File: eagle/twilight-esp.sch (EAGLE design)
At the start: 12 parts, among them J1 Mini PIR, J2 VOUT, J3 VIN, Q1 IRF540, U1 7805

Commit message: add led
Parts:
- added D1: (no value), SparkFun-LED:LED3MM
- added R5: 220R, resistor:R-EU_0204/5
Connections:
- new net N$6: R5.1, WEMOS1.D2
- new net N$7: D1.C, R5.2
- net 3.3V: now also D1.A
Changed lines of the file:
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@@
 <part name="SUPPLY8" library="SparkFun-PowerSymbols" deviceset="12V" device=""/>
 <part name="GND8" library="SparkFun-PowerSymbols" deviceset="GND" device=""/>
+<part name="R5" library="resistor" deviceset="R-EU_" device="0204/5" value="220R"/>
+<part name="D1" library="SparkFun-LED" deviceset="LED" device="3MM"/>
+<part name="SUPPLY9" library="SparkFun-PowerSymbols" deviceset="3.3V" device=""/>
 </parts>
 <sheets>
@@
 <instance part="SUPPLY8" gate="G$1" x="-2.54" y="45.72"/>
 <instance part="GND8" gate="1" x="-2.54" y="33.02"/>
+<instance part="R5" gate="G$1" x="68.58" y="76.2" rot="R90"/>
+<instance part="D1" gate="G$1" x="68.58" y="86.36"/>
+<instance part="SUPPLY9" gate="G$1" x="68.58" y="88.9"/>
 </instances>
 <busses>
@@
 <wire x1="15.24" y1="68.58" x2="15.24" y2="71.12" width="0.1524" layer="91"/>
 </segment>
+<segment>
+<wire x1="17.78" y1="60.96" x2="17.78" y2="63.5" width="0.1524" layer="91"/>
+</segment>
 </net>
 <net name="N$3" class="0">
@@
 <pinref part="SUPPLY2" gate="G$1" pin="3.3V"/>
 </segment>
+<segment>
+<pinref part="D1" gate="G$1" pin="A"/>
+<pinref part="SUPPLY9" gate="G$1" pin="3.3V"/>
+</segment>
 </net>
 <net name="5V" class="0">
@@
 </segment>
 </net>
+<net name="N$6" class="0">
+<segment>
+<pinref part="WEMOS1" gate="D1" pin="D2"/>
+<pinref part="R5" gate="G$1" pin="1"/>
+<wire x1="60.96" y1="71.12" x2="68.58" y2="71.12" width="0.1524" layer="91"/>
+</segment>
+</net>
+<net name="N$7" class="0">
+<segment>
+<pinref part="R5" gate="G$1" pin="2"/>
+<pinref part="D1" gate="G$1" pin="C"/>
+</segment>
+</net>

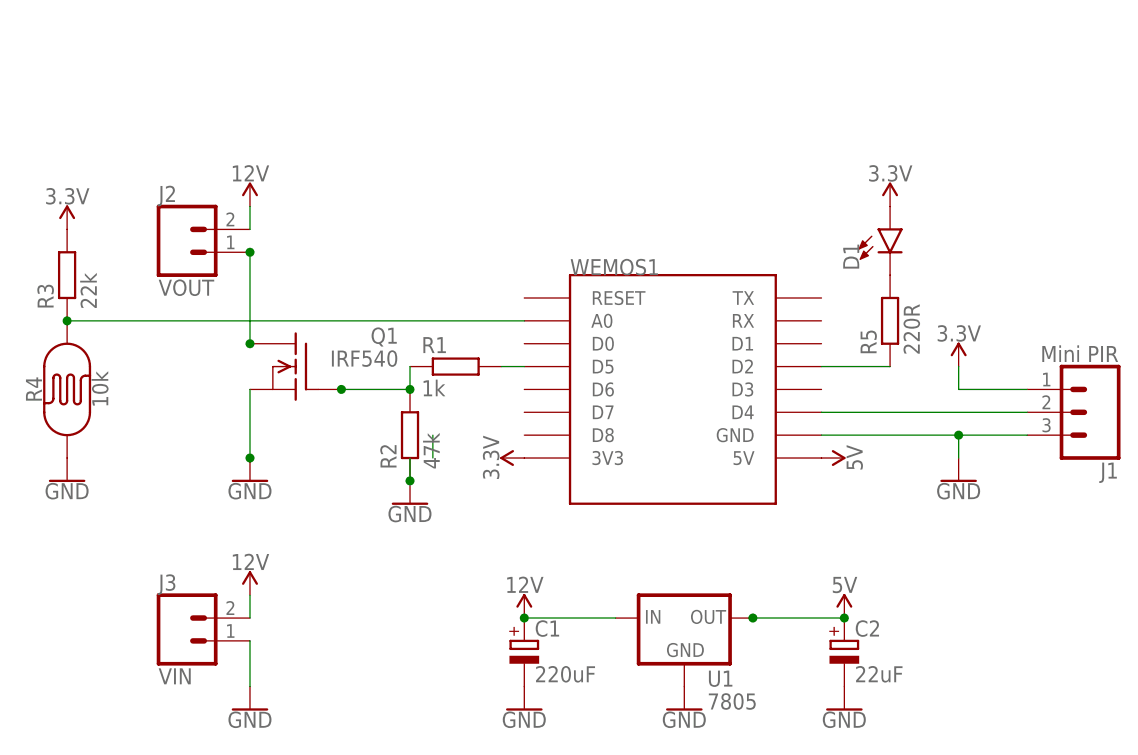
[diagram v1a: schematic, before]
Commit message: update schematic
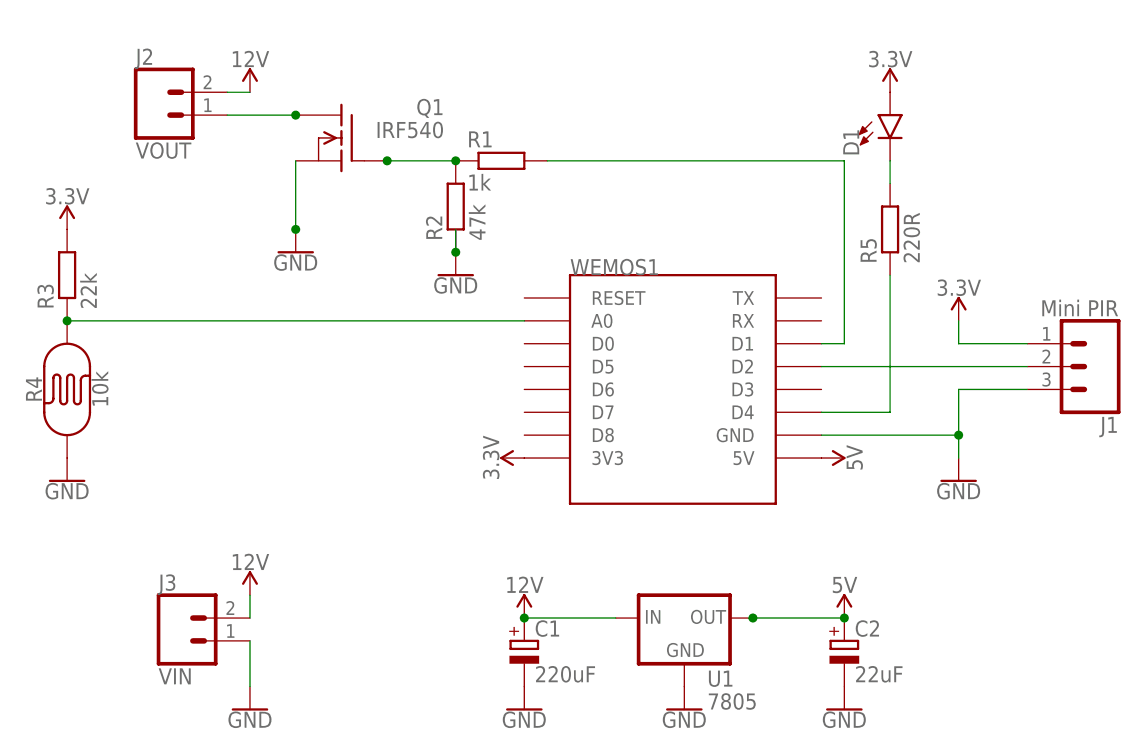
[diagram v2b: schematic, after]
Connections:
- net N$1: now also WEMOS1.D1; no longer WEMOS1.D5
- net N$4: now also R5.1; no longer J1.2
- net N$6: now also J1.2; no longer R5.1
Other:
- moved on the sheet: D1, J1, J2, Q1, R1, R2, R5
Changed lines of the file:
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@@
 <instances>
 <instance part="WEMOS1" gate="D1" x="43.18" y="68.58"/>
-<instance part="R1" gate="G$1" x="20.32" y="71.12"/>
-<instance part="R2" gate="G$1" x="15.24" y="63.5" rot="R90"/>
+<instance part="R1" gate="G$1" x="25.4" y="93.98"/>
+<instance part="R2" gate="G$1" x="20.32" y="88.9" rot="R90"/>
 <instance part="R3" gate="G$1" x="-22.86" y="81.28" rot="R90"/>
-<instance part="Q1" gate="G$1" x="2.54" y="71.12" rot="MR0"/>
+<instance part="Q1" gate="G$1" x="7.62" y="96.52" rot="MR0"/>
 <instance part="R4" gate="G$1" x="-22.86" y="68.58" rot="R90"/>
 <instance part="GND3" gate="1" x="76.2" y="58.42"/>
-<instance part="GND5" gate="1" x="-2.54" y="58.42"/>
+<instance part="GND5" gate="1" x="2.54" y="83.82"/>
 <instance part="SUPPLY1" gate="G$1" x="-22.86" y="86.36"/>
 <instance part="SUPPLY2" gate="G$1" x="27.94" y="60.96" rot="R90"/>
 <instance part="SUPPLY3" gate="G$1" x="60.96" y="60.96" rot="R270"/>
-<instance part="J1" gate="J$1" x="91.44" y="66.04" rot="R180"/>
-<instance part="SUPPLY4" gate="G$1" x="76.2" y="71.12"/>
-<instance part="J2" gate="G$1" x="-10.16" y="83.82"/>
+<instance part="J1" gate="J$1" x="91.44" y="71.12" rot="R180"/>
+<instance part="SUPPLY4" gate="G$1" x="76.2" y="76.2"/>
+<instance part="J2" gate="G$1" x="-12.7" y="99.06"/>
 <instance part="GND2" gate="1" x="-22.86" y="58.42"/>
-<instance part="GND1" gate="1" x="15.24" y="55.88"/>
-<instance part="SUPPLY5" gate="G$1" x="-2.54" y="88.9"/>
+<instance part="GND1" gate="1" x="20.32" y="81.28"/>
+<instance part="SUPPLY5" gate="G$1" x="-2.54" y="101.6"/>
 <instance part="U1" gate="G$1" x="45.72" y="43.18"/>
 <instance part="SUPPLY6" gate="G$1" x="27.94" y="43.18"/>
@@
 <instance part="SUPPLY8" gate="G$1" x="-2.54" y="45.72"/>
 <instance part="GND8" gate="1" x="-2.54" y="33.02"/>
-<instance part="R5" gate="G$1" x="68.58" y="76.2" rot="R90"/>
-<instance part="D1" gate="G$1" x="68.58" y="86.36"/>
-<instance part="SUPPLY9" gate="G$1" x="68.58" y="88.9"/>
+<instance part="R5" gate="G$1" x="68.58" y="86.36" rot="R90"/>
+<instance part="D1" gate="G$1" x="68.58" y="99.06"/>
+<instance part="SUPPLY9" gate="G$1" x="68.58" y="101.6"/>
 </instances>
 <busses>
 </busses>
 <nets>
-<net name="N$1" class="0">
-<segment>
-<pinref part="WEMOS1" gate="D1" pin="D5"/>
-<pinref part="R1" gate="G$1" pin="2"/>
-<wire x1="25.4" y1="71.12" x2="27.94" y2="71.12" width="0.1524" layer="91"/>
-</segment>
-</net>
-<net name="N$2" class="0">
-<segment>
-<pinref part="R1" gate="G$1" pin="1"/>
-<pinref part="R2" gate="G$1" pin="2"/>
-<pinref part="Q1" gate="G$1" pin="G"/>
-<junction x="7.62" y="68.58"/>
-<pinref part="Q1" gate="G$1" pin="G"/>
-<wire x1="7.62" y1="68.58" x2="15.24" y2="68.58" width="0.1524" layer="91"/>
-<junction x="15.24" y="68.58"/>
-<wire x1="15.24" y1="68.58" x2="15.24" y2="71.12" width="0.1524" layer="91"/>
-</segment>
-<segment>
-<wire x1="17.78" y1="60.96" x2="17.78" y2="63.5" width="0.1524" layer="91"/>
-</segment>
-</net>
 <net name="N$3" class="0">
 <segment>
@@
 <wire x1="76.2" y1="63.5" x2="76.2" y2="60.96" width="0.1524" layer="91"/>
 <pinref part="J1" gate="J$1" pin="3"/>
-<wire x1="76.2" y1="63.5" x2="83.82" y2="63.5" width="0.1524" layer="91"/>
+<wire x1="76.2" y1="63.5" x2="76.2" y2="68.58" width="0.1524" layer="91"/>
+<wire x1="76.2" y1="68.58" x2="83.82" y2="68.58" width="0.1524" layer="91"/>
 <junction x="76.2" y="63.5"/>
 </segment>
@@
 <pinref part="Q1" gate="G$1" pin="S"/>
 <pinref part="GND5" gate="1" pin="GND"/>
-<wire x1="-2.54" y1="68.58" x2="-2.54" y2="60.96" width="0.1524" layer="91"/>
-<junction x="-2.54" y="60.96"/>
+<wire x1="2.54" y1="93.98" x2="2.54" y2="86.36" width="0.1524" layer="91"/>
+<junction x="2.54" y="86.36"/>
 </segment>
 <segment>
 <pinref part="R2" gate="G$1" pin="1"/>
-<wire x1="15.24" y1="58.42" x2="15.24" y2="60.96" width="0.1524" layer="91"/>
+<wire x1="20.32" y1="83.82" x2="20.32" y2="86.36" width="0.1524" layer="91"/>
 <pinref part="GND1" gate="1" pin="GND"/>
-<junction x="15.24" y="58.42"/>
+<junction x="20.32" y="83.82"/>
 </segment>
 <segment>
@@
 <pinref part="J1" gate="J$1" pin="1"/>
 <pinref part="SUPPLY4" gate="G$1" pin="3.3V"/>
-<wire x1="76.2" y1="71.12" x2="76.2" y2="68.58" width="0.1524" layer="91"/>
-<wire x1="76.2" y1="68.58" x2="83.82" y2="68.58" width="0.1524" layer="91"/>
+<wire x1="76.2" y1="76.2" x2="76.2" y2="73.66" width="0.1524" layer="91"/>
+<wire x1="76.2" y1="73.66" x2="83.82" y2="73.66" width="0.1524" layer="91"/>
 </segment>
 <segment>
@@
 </segment>
 </net>
-<net name="N$4" class="0">
-<segment>
-<pinref part="WEMOS1" gate="D1" pin="D4"/>
-<pinref part="J1" gate="J$1" pin="2"/>
-<wire x1="60.96" y1="66.04" x2="83.82" y2="66.04" width="0.1524" layer="91"/>
-</segment>
-</net>
 <net name="N$5" class="0">
 <segment>
 <pinref part="J2" gate="G$1" pin="1"/>
 <pinref part="Q1" gate="G$1" pin="D"/>
-<wire x1="-2.54" y1="83.82" x2="-2.54" y2="73.66" width="0.1524" layer="91"/>
-<junction x="-2.54" y="83.82"/>
-<junction x="-2.54" y="73.66"/>
+<wire x1="-5.08" y1="99.06" x2="2.54" y2="99.06" width="0.1524" layer="91"/>
+<junction x="2.54" y="99.06"/>
 </segment>
 </net>
@@
 <pinref part="SUPPLY5" gate="G$1" pin="12V"/>
 <pinref part="J2" gate="G$1" pin="2"/>
-<wire x1="-2.54" y1="88.9" x2="-2.54" y2="86.36" width="0.1524" layer="91"/>
+<wire x1="-2.54" y1="101.6" x2="-5.08" y2="101.6" width="0.1524" layer="91"/>
 </segment>
 <segment>
@@
 </segment>
 </net>
-<net name="N$6" class="0">
-<segment>
-<pinref part="WEMOS1" gate="D1" pin="D2"/>
-<pinref part="R5" gate="G$1" pin="1"/>
-<wire x1="60.96" y1="71.12" x2="68.58" y2="71.12" width="0.1524" layer="91"/>
-</segment>
-</net>
 <net name="N$7" class="0">
 <segment>
 <pinref part="R5" gate="G$1" pin="2"/>
 <pinref part="D1" gate="G$1" pin="C"/>
+<wire x1="68.58" y1="93.98" x2="68.58" y2="91.44" width="0.1524" layer="91"/>
 </segment>
 </net>
+<net name="N$4" class="0">
+<segment>
+<pinref part="WEMOS1" gate="D1" pin="D4"/>
+<wire x1="60.96" y1="66.04" x2="68.58" y2="66.04" width="0.1524" layer="91"/>
+<pinref part="R5" gate="G$1" pin="1"/>
+<wire x1="68.58" y1="66.04" x2="68.58" y2="81.28" width="0.1524" layer="91"/>
+</segment>
+</net>
+<net name="N$6" class="0">
+<segment>
+<pinref part="WEMOS1" gate="D1" pin="D2"/>
+<pinref part="J1" gate="J$1" pin="2"/>
+<wire x1="60.96" y1="71.12" x2="83.82" y2="71.12" width="0.1524" layer="91"/>
+</segment>
+</net>
+<net name="N$1" class="0">
+<segment>
+<pinref part="R1" gate="G$1" pin="2"/>
+<wire x1="30.48" y1="93.98" x2="63.5" y2="93.98" width="0.1524" layer="91"/>
+<wire x1="63.5" y1="93.98" x2="63.5" y2="73.66" width="0.1524" layer="91"/>
+<pinref part="WEMOS1" gate="D1" pin="D1"/>
+<wire x1="60.96" y1="73.66" x2="63.5" y2="73.66" width="0.1524" layer="91"/>
+</segment>
+</net>
+<net name="N$2" class="0">
+<segment>
+<pinref part="Q1" gate="G$1" pin="G"/>
+<pinref part="Q1" gate="G$1" pin="G"/>
+<pinref part="R1" gate="G$1" pin="1"/>
+<pinref part="R2" gate="G$1" pin="2"/>
+<wire x1="12.7" y1="93.98" x2="20.32" y2="93.98" width="0.1524" layer="91"/>
+<junction x="12.7" y="93.98"/>
+<junction x="20.32" y="93.98"/>
+</segment>
+</net>

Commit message: config on/off_delay
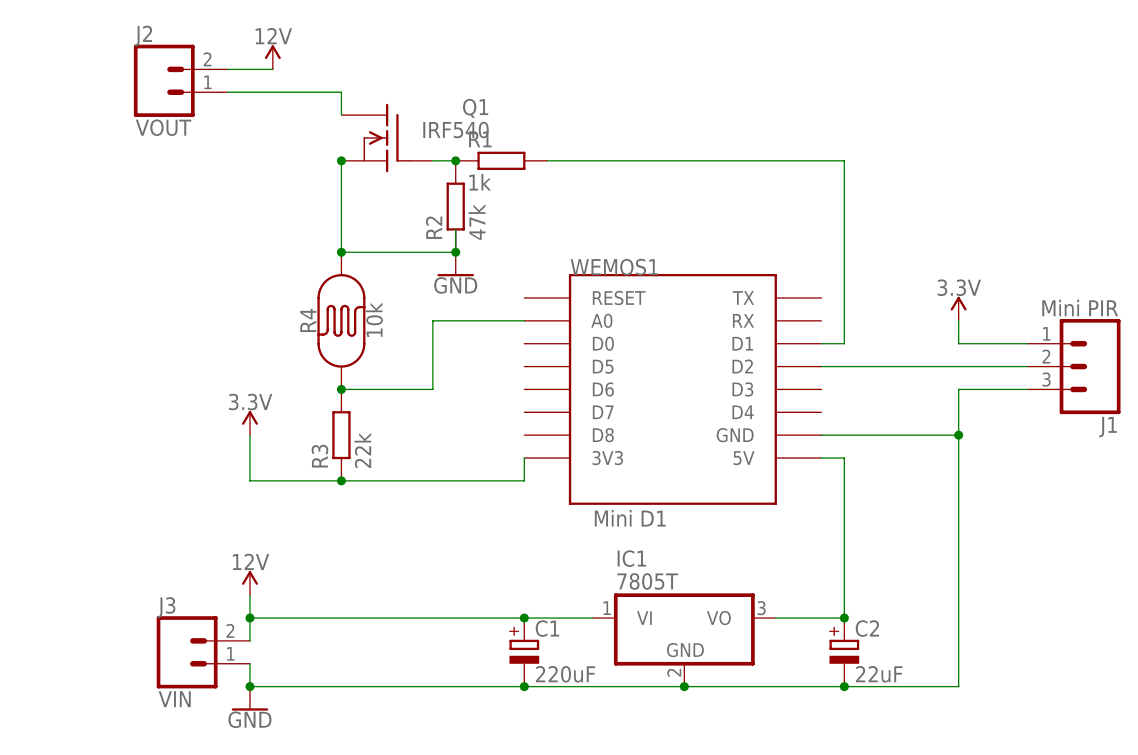
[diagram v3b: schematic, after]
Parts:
- removed D1: (no value), SparkFun-LED:LED3MM
- removed R5: 220R, resistor:R-EU_0204/5
- removed U1: 7805, SparkFun-IC-Power:V_REG_78XXSINK
- added IC1: 7805T, linear:7805T
- WEMOS1: value (none) -> Mini D1
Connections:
- removed net 5V: C2.+, U1.OUT, WEMOS1.5V
- removed net N$4: R5.1, WEMOS1.D4
- removed net N$7: D1.C, R5.2
- new net N$8: C2.+, IC1.VO, WEMOS1.5V
- net 12V: now also IC1.VI; no longer U1.IN
- net 3.3V: now also R3.1; no longer D1.A, R3.2
- net GND: now also IC1.GND, R4.P$2; no longer R4.P$1, U1.GND
- net N$3: now also R3.2, R4.P$1; no longer R3.1, R4.P$2
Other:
- moved on the sheet: J2, J3, Q1, R3, R4

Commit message: add start state; flash pir led
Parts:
- R1, R2, R3: device resistor:R-EU_0204/5 -> rcl:R-EU_0207/7
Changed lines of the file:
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@@
 <parts>
 <part name="WEMOS1" library="esp8266modules" deviceset="WEMOS-D1-MINI" device="" value="Mini D1"/>
-<part name="R1" library="resistor" deviceset="R-EU_" device="0204/5" value="1k"/>
-<part name="R2" library="resistor" deviceset="R-EU_" device="0204/5" value="47k"/>
-<part name="R3" library="resistor" deviceset="R-EU_" device="0204/5" value="22k"/>
 <part name="R4" library="SparkFun-Sensors" deviceset="PHOTOCELL" device="PTH" value="10k"/>
 <part name="J1" library="SparkFun-Connectors" deviceset="CONN_03" device="" value="Mini PIR"/>
@@
 <part name="IC1" library="linear" deviceset="78*" device="T" technology="05"/>
 <part name="Q1" library="transistor-fet" deviceset="IRF540" device=""/>
+<part name="R1" library="rcl" deviceset="R-EU_" device="0207/7" value="1k"/>
+<part name="R2" library="rcl" deviceset="R-EU_" device="0207/7" value="47k"/>
+<part name="R3" library="rcl" deviceset="R-EU_" device="0207/7" value="22k"/>
 </parts>
 <sheets>
@@
 <instances>
 <instance part="WEMOS1" gate="D1" x="43.18" y="68.58"/>
-<instance part="R1" gate="G$1" x="25.4" y="93.98"/>
-<instance part="R2" gate="G$1" x="20.32" y="88.9" rot="R90"/>
-<instance part="R3" gate="G$1" x="7.62" y="63.5" rot="R90"/>
 <instance part="R4" gate="G$1" x="7.62" y="76.2" rot="R90"/>
 <instance part="J1" gate="J$1" x="91.44" y="71.12" rot="R180"/>
@@
 <instance part="IC1" gate="A1" x="45.72" y="43.18"/>
 <instance part="Q1" gate="G$1" x="12.7" y="96.52" rot="MR0"/>
+<instance part="R1" gate="G$1" x="25.4" y="93.98"/>
+<instance part="R2" gate="G$1" x="20.32" y="88.9" rot="R90"/>
+<instance part="R3" gate="G$1" x="7.62" y="63.5" rot="R90"/>
 </instances>
 <busses>
@@
 </segment>
 <segment>
-<pinref part="R2" gate="G$1" pin="1"/>
 <wire x1="20.32" y1="83.82" x2="20.32" y2="86.36" width="0.1524" layer="91"/>
 <junction x="20.32" y="83.82"/>
@@
 <pinref part="Q1" gate="G$1" pin="S"/>
 <junction x="7.62" y="93.98"/>
+<pinref part="R2" gate="G$1" pin="1"/>
 </segment>
 </net>
@@
 <pinref part="WEMOS1" gate="D1" pin="3V3"/>
 <wire x1="27.94" y1="60.96" x2="27.94" y2="58.42" width="0.1524" layer="91"/>
-<pinref part="R3" gate="G$1" pin="1"/>
 <wire x1="27.94" y1="58.42" x2="7.62" y2="58.42" width="0.1524" layer="91"/>
 <wire x1="7.62" y1="58.42" x2="-2.54" y2="58.42" width="0.1524" layer="91"/>
 <wire x1="-2.54" y1="58.42" x2="-2.54" y2="63.5" width="0.1524" layer="91"/>
 <pinref part="SUPPLY1" gate="G$1" pin="3.3V"/>
+<pinref part="R3" gate="G$1" pin="1"/>
 <junction x="7.62" y="58.42"/>
 </segment>
@@
 <net name="N$1" class="0">
 <segment>
-<pinref part="R1" gate="G$1" pin="2"/>
 <wire x1="30.48" y1="93.98" x2="63.5" y2="93.98" width="0.1524" layer="91"/>
 <wire x1="63.5" y1="93.98" x2="63.5" y2="73.66" width="0.1524" layer="91"/>
 <pinref part="WEMOS1" gate="D1" pin="D1"/>
 <wire x1="60.96" y1="73.66" x2="63.5" y2="73.66" width="0.1524" layer="91"/>
+<pinref part="R1" gate="G$1" pin="2"/>
 </segment>
 </net>
 <net name="N$2" class="0">
 <segment>
+<pinref part="Q1" gate="G$1" pin="G"/>
+<wire x1="17.78" y1="93.98" x2="20.32" y2="93.98" width="0.1524" layer="91"/>
 <pinref part="R1" gate="G$1" pin="1"/>
 <pinref part="R2" gate="G$1" pin="2"/>
-<pinref part="Q1" gate="G$1" pin="G"/>
-<wire x1="17.78" y1="93.98" x2="20.32" y2="93.98" width="0.1524" layer="91"/>
 <junction x="20.32" y="93.98"/>
 </segment>
@@
 <segment>
 <pinref part="R4" gate="G$1" pin="P$1"/>
-<pinref part="R3" gate="G$1" pin="2"/>
 <wire x1="7.62" y1="68.58" x2="17.78" y2="68.58" width="0.1524" layer="91"/>
 <wire x1="17.78" y1="68.58" x2="17.78" y2="76.2" width="0.1524" layer="91"/>
 <pinref part="WEMOS1" gate="D1" pin="A0"/>
 <wire x1="17.78" y1="76.2" x2="27.94" y2="76.2" width="0.1524" layer="91"/>
+<pinref part="R3" gate="G$1" pin="2"/>
 <junction x="7.62" y="68.58"/>
 </segment>

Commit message: add reset header
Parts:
- added JP1: RESET, pinhead:PINHD-1X2
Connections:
- new net N$4: JP1.1, WEMOS1.RESET
- net GND: now also JP1.2
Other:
- moved on the sheet: R1
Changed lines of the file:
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@@
 <part name="R2" library="rcl" deviceset="R-EU_" device="0207/7" value="47k"/>
 <part name="R3" library="rcl" deviceset="R-EU_" device="0207/7" value="22k"/>
+<part name="JP1" library="pinhead" deviceset="PINHD-1X2" device="" value="RESET"/>
+<part name="GND2" library="SparkFun-PowerSymbols" deviceset="GND" device=""/>
 </parts>
 <sheets>
@@
 <instance part="IC1" gate="A1" x="45.72" y="43.18"/>
 <instance part="Q1" gate="G$1" x="12.7" y="96.52" rot="MR0"/>
-<instance part="R1" gate="G$1" x="25.4" y="93.98"/>
+<instance part="R1" gate="G$1" x="38.1" y="93.98"/>
 <instance part="R2" gate="G$1" x="20.32" y="88.9" rot="R90"/>
 <instance part="R3" gate="G$1" x="7.62" y="63.5" rot="R90"/>
+<instance part="JP1" gate="G$1" x="91.44" y="96.52"/>
+<instance part="GND2" gate="1" x="76.2" y="91.44"/>
 </instances>
 <busses>
@@
 <junction x="7.62" y="93.98"/>
 <pinref part="R2" gate="G$1" pin="1"/>
+</segment>
+<segment>
+<pinref part="GND2" gate="1" pin="GND"/>
+<wire x1="73.66" y1="91.44" x2="76.2" y2="91.44" width="0.1524" layer="91"/>
+<wire x1="76.2" y1="91.44" x2="76.2" y2="93.98" width="0.1524" layer="91"/>
+<wire x1="76.2" y1="93.98" x2="76.2" y2="96.52" width="0.1524" layer="91"/>
+<pinref part="JP1" gate="G$1" pin="2"/>
+<wire x1="76.2" y1="96.52" x2="88.9" y2="96.52" width="0.1524" layer="91"/>
+<junction x="76.2" y="93.98"/>
 </segment>
 </net>
@@
 <net name="N$1" class="0">
 <segment>
-<wire x1="30.48" y1="93.98" x2="63.5" y2="93.98" width="0.1524" layer="91"/>
+<wire x1="43.18" y1="93.98" x2="63.5" y2="93.98" width="0.1524" layer="91"/>
 <wire x1="63.5" y1="93.98" x2="63.5" y2="73.66" width="0.1524" layer="91"/>
 <pinref part="WEMOS1" gate="D1" pin="D1"/>
@@
 <segment>
 <pinref part="Q1" gate="G$1" pin="G"/>
-<wire x1="17.78" y1="93.98" x2="20.32" y2="93.98" width="0.1524" layer="91"/>
+<wire x1="17.78" y1="93.98" x2="33.02" y2="93.98" width="0.1524" layer="91"/>
 <pinref part="R1" gate="G$1" pin="1"/>
 <pinref part="R2" gate="G$1" pin="2"/>
-<junction x="20.32" y="93.98"/>
+<junction x="33.02" y="93.98"/>
+<wire x1="33.02" y1="93.98" x2="20.32" y2="93.98" width="0.1524" layer="91"/>
 </segment>
 </net>
@@
 </segment>
 </net>
+<net name="N$4" class="0">
+<segment>
+<pinref part="WEMOS1" gate="D1" pin="RESET"/>
+<wire x1="27.94" y1="78.74" x2="27.94" y2="99.06" width="0.1524" layer="91"/>
+<pinref part="JP1" gate="G$1" pin="1"/>
+<wire x1="27.94" y1="99.06" x2="88.9" y2="99.06" width="0.1524" layer="91"/>
+</segment>
+</net>
